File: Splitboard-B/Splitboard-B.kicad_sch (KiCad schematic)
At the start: 83 parts

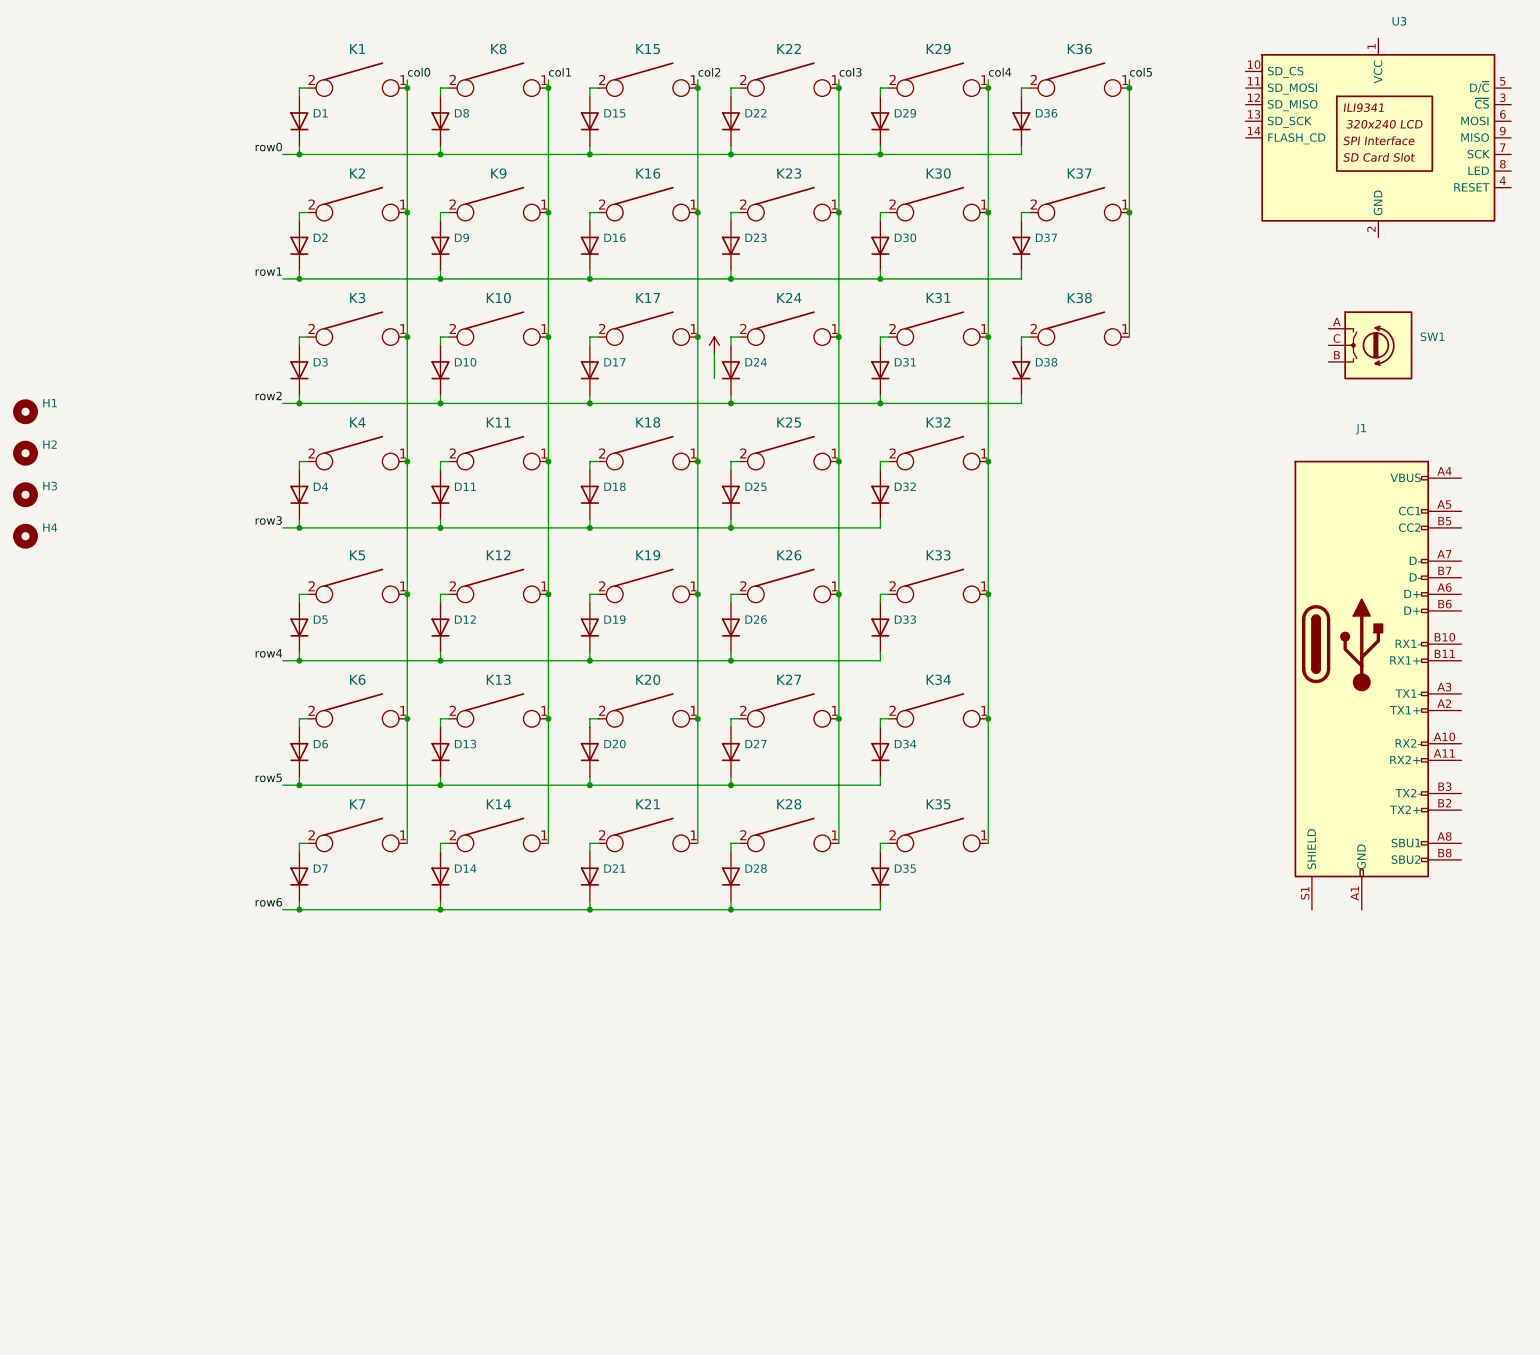
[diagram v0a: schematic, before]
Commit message: Keyboard changes (added split to other half, component footprints)
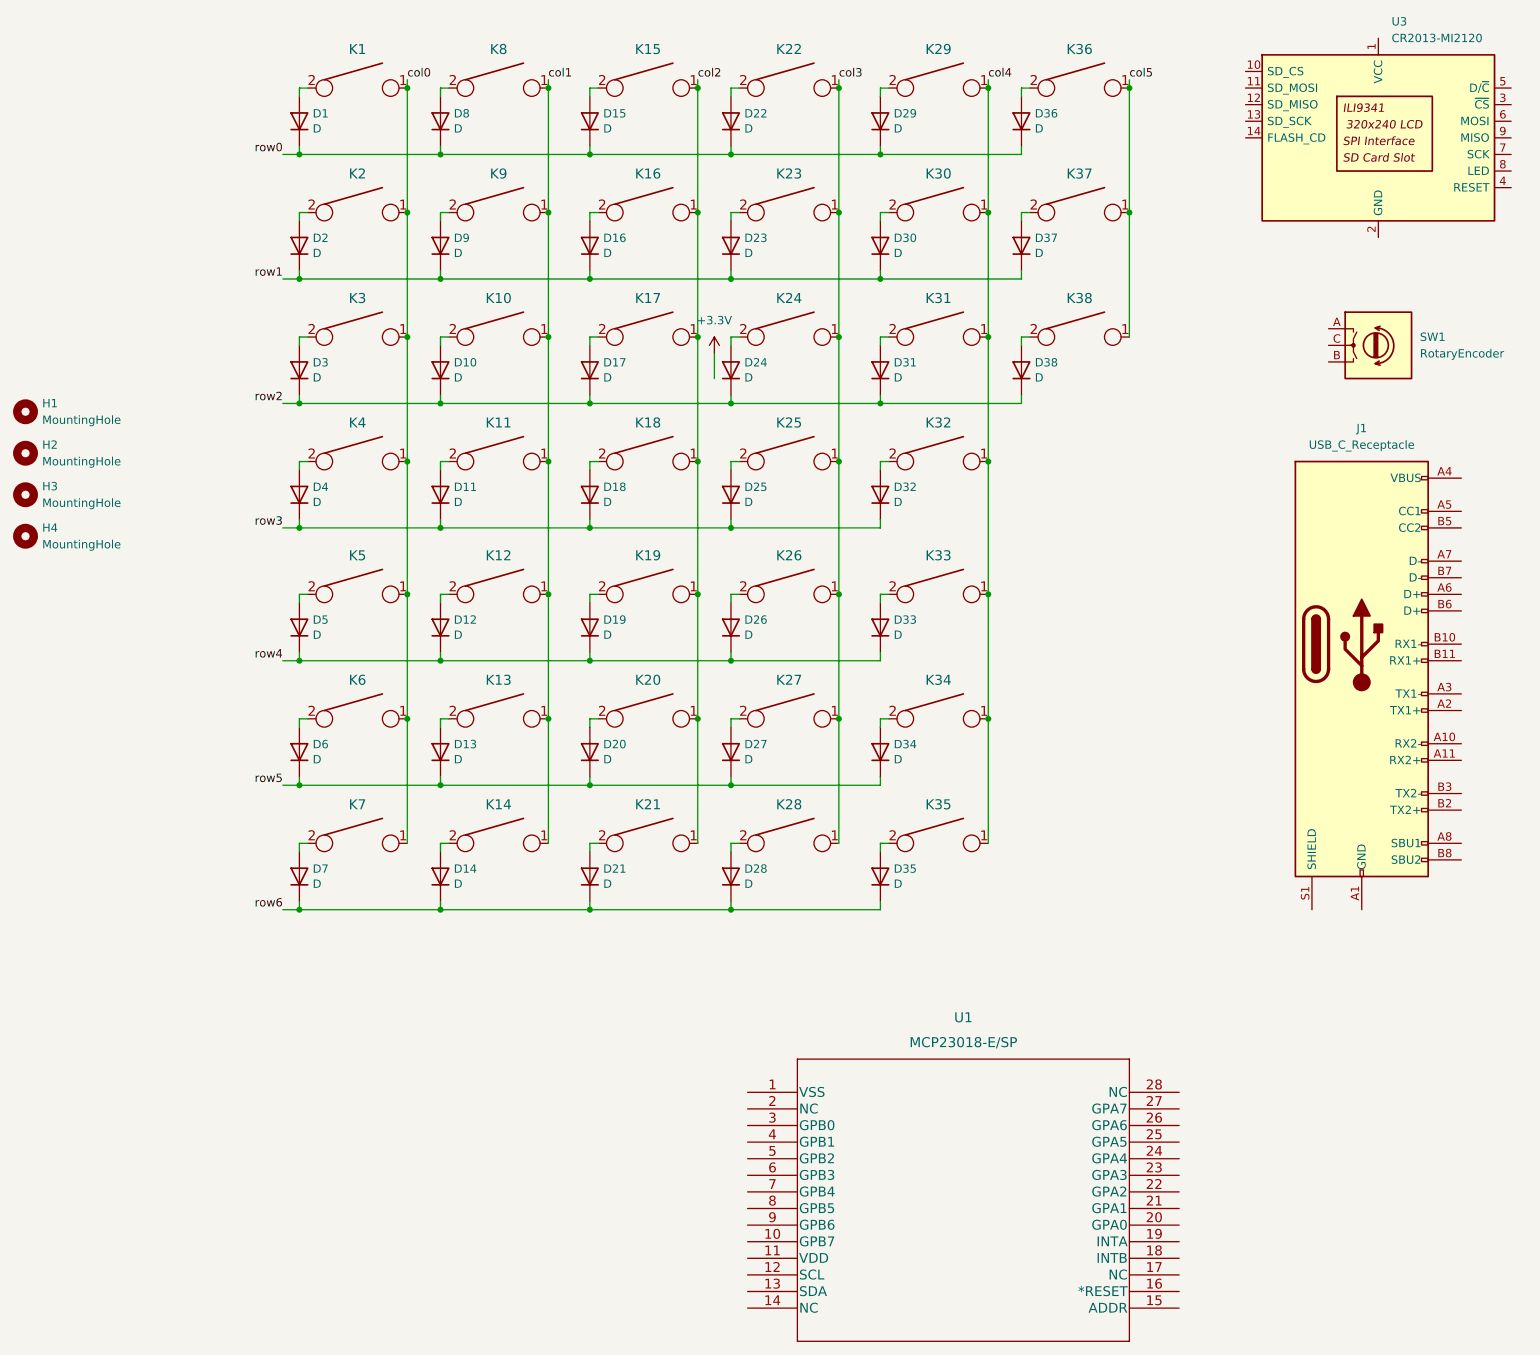
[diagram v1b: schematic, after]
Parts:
- added U1: MCP23018-E/SP, 6:MCP23018-E&slash_SP, symbol Interface_Expansion:MCP23018-E{brace}slash}SP
- D1, D10, D11, D12, D13, D14, D15, D16, D17, D18, D19, D2, D20, D21, D22, D23, D24, D25, D26, D27, D28, D29, D3, D30, D31, D32, D33, D34, D35, D36, D37, D38, D4, D5, D6, D7, D8, D9: value (none) -> D; footprint (none) -> Diode_SMD:D_SOD-123
- H1, H2, H3, H4: value (none) -> MountingHole; footprint (none) -> MountingHole:MountingHole_2.7mm
- J1: value (none) -> USB_C_Receptacle; footprint (none) -> USB_C_Receptacle_GCT_USB4085
- K1, K10, K11, K12, K13, K14, K15, K16, K17, K18, K19, K2, K20, K21, K22, K23, K24, K25, K26, K27, K28, K29, K3, K30, K31, K32, K33, K34, K35, K36, K37, K38, K4, K5, K6, K7, K8, K9: value (none) -> KEYSW; footprint (none) -> 6:SW_Hotswap_Kailh_MX_plated
- SW1: value (none) -> RotaryEncoder; footprint (none) -> Rotary_Encoder:RotaryEncoder_Alps_EC12E_Vertical_H20mm
- U3: value (none) -> CR2013-MI2120; footprint (none) -> Display:CR2013-MI2120

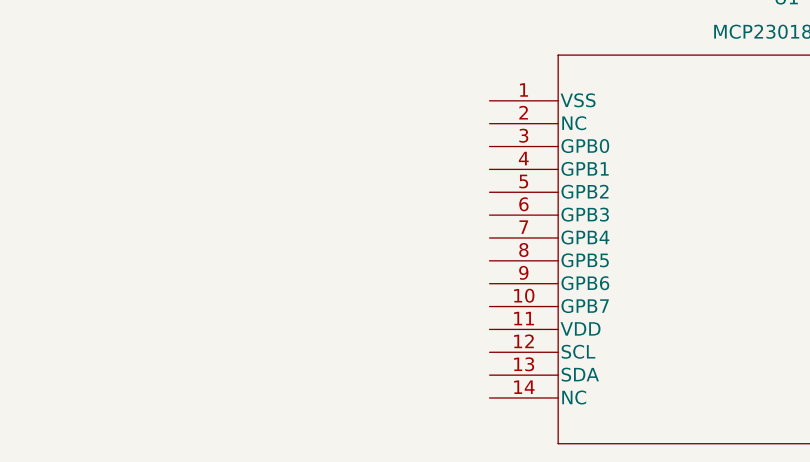
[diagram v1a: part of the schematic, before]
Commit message: added pullup resisitors
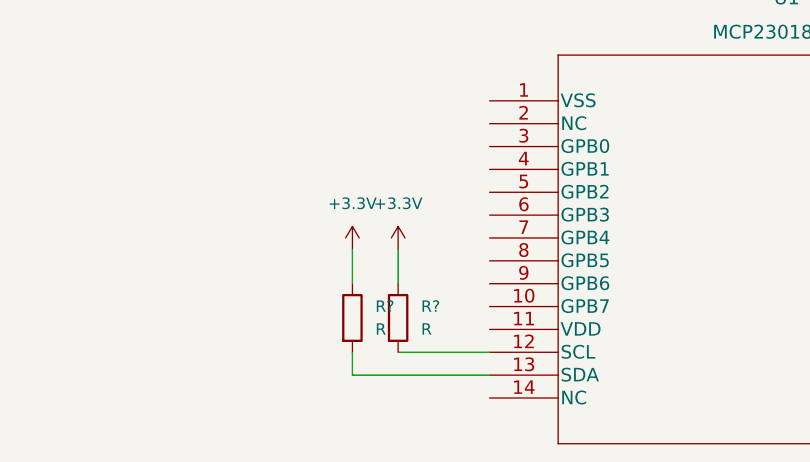
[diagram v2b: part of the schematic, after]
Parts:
- added R? (x2): R, symbol Device:R
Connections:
- net +3.3V: now also R?.1, R?.1
- net at U1.12 (SCL): now also R?.2
- net at U1.13 (SDA): now also R?.2
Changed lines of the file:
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@@
+    (stroke (width 0) (type default) (color 0 0 0 0))
+  )
+  (wire (pts (xy 133.35 218.44) (xy 118.11 218.44))
     (stroke (width 0) (type default) (color 0 0 0 0))
   )
@@
     (stroke (width 0) (type default) (color 0 0 0 0))
   )
+  (wire (pts (xy 123.19 204.47) (xy 123.19 208.28))
+    (stroke (width 0) (type default) (color 0 0 0 0))
+  )
   (wire (pts (xy 87.63 91.44) (xy 86.36 91.44))
     (stroke (width 0) (type default) (color 0 0 0 0))
@@
     (stroke (width 0) (type default) (color 0 0 0 0))
   )
+  (wire (pts (xy 118.11 215.9) (xy 118.11 218.44))
+    (stroke (width 0) (type default) (color 0 0 0 0))
+  )
   (wire (pts (xy 109.22 63.5) (xy 130.81 63.5))
     (stroke (width 0) (type default) (color 0 0 0 0))
@@
     (stroke (width 0) (type default) (color 0 0 0 0))
   )
+  (wire (pts (xy 123.19 215.9) (xy 133.35 215.9))
+    (stroke (width 0) (type default) (color 0 0 0 0))
+  )
   (wire (pts (xy 109.22 120.65) (xy 109.22 121.92))
     (stroke (width 0) (type default) (color 0 0 0 0))
@@
   )
   (wire (pts (xy 130.81 149.86) (xy 130.81 151.13))
+    (stroke (width 0) (type default) (color 0 0 0 0))
+  )
+  (wire (pts (xy 118.11 204.47) (xy 118.11 208.28))
     (stroke (width 0) (type default) (color 0 0 0 0))
   )
@@
     (pin "1")
     (pin "2")
+  )
+  (symbol (lib_id "power:+3.3V") (at 118.11 204.47 0) (unit 1)
+    (in_bom yes) (on_board yes) (fields_autoplaced)
+    (property "Reference" "#PWR?" (id 0) (at 118.11 208.28 0)
+      (effects (font (size 1.27 1.27)) hide)
+    )
+    (property "Value" "+3.3V" (id 1) (at 118.11 199.39 0))
+    (property "Footprint" "" (id 2) (at 118.11 204.47 0)
+      (effects (font (size 1.27 1.27)) hide)
+    )
+    (property "Datasheet" "" (id 3) (at 118.11 204.47 0)
+      (effects (font (size 1.27 1.27)) hide)
+    )
+    (pin "1")
   )
   (symbol (lib_id "KBT1-rescue:D-Device") (at 64.77 135.89 90) (unit 1)
@@
     (pin "2")
   )
+  (symbol (lib_id "power:+3.3V") (at 123.19 204.47 0) (unit 1)
+    (in_bom yes) (on_board yes) (fields_autoplaced)
+    (property "Reference" "#PWR?" (id 0) (at 123.19 208.28 0)
+      (effects (font (size 1.27 1.27)) hide)
+    )
+    (property "Value" "+3.3V" (id 1) (at 123.19 199.39 0))
+    (property "Footprint" "" (id 2) (at 123.19 204.47 0)
+      (effects (font (size 1.27 1.27)) hide)
+    )
+    (property "Datasheet" "" (id 3) (at 123.19 204.47 0)
+      (effects (font (size 1.27 1.27)) hide)
+    )
+    (pin "1")
+  )
   (symbol (lib_id "Mechanical:MountingHole") (at 22.86 96.52 0) (unit 1)
     (in_bom yes) (on_board yes) (fields_autoplaced)
@@
       (effects (font (size 1.27 1.27)) hide)
     )
+  )
+  (symbol (lib_id "Device:R") (at 118.11 212.09 0) (unit 1)
+    (in_bom yes) (on_board yes) (fields_autoplaced)
+    (property "Reference" "R?" (id 0) (at 120.65 210.8199 0)
+      (effects (font (size 1.27 1.27)) (justify left))
+    )
+    (property "Value" "R" (id 1) (at 120.65 213.3599 0)
+      (effects (font (size 1.27 1.27)) (justify left))
+    )
+    (property "Footprint" "" (id 2) (at 116.332 212.09 90)
+      (effects (font (size 1.27 1.27)) hide)
+    )
+    (property "Datasheet" "~" (id 3) (at 118.11 212.09 0)
+      (effects (font (size 1.27 1.27)) hide)
+    )
+    (pin "1")
+    (pin "2")
   )
   (symbol (lib_id "Mechanical:MountingHole") (at 22.86 102.87 0) (unit 1)
@@
     (property "Datasheet" "" (id 3) (at 162.56 53.34 0)
       (effects (font (size 1.524 1.524)))
+    )
+    (pin "1")
+    (pin "2")
+  )
+  (symbol (lib_id "Device:R") (at 123.19 212.09 0) (unit 1)
+    (in_bom yes) (on_board yes) (fields_autoplaced)
+    (property "Reference" "R?" (id 0) (at 125.73 210.8199 0)
+      (effects (font (size 1.27 1.27)) (justify left))
+    )
+    (property "Value" "R" (id 1) (at 125.73 213.3599 0)
+      (effects (font (size 1.27 1.27)) (justify left))
+    )
+    (property "Footprint" "" (id 2) (at 121.412 212.09 90)
+      (effects (font (size 1.27 1.27)) hide)
+    )
+    (property "Datasheet" "~" (id 3) (at 123.19 212.09 0)
+      (effects (font (size 1.27 1.27)) hide)
     )
     (pin "1")
@@
       (reference "#PWR0103") (unit 1) (value "+3.3V") (footprint "")
     )
+    (path "/31e77a53-3db0-43d9-8c57-a14833466fba"
+      (reference "#PWR?") (unit 1) (value "+3.3V") (footprint "")
+    )
+    (path "/5900d3e4-ddc5-4aff-8a88-379afa05c05c"
+      (reference "#PWR?") (unit 1) (value "+3.3V") (footprint "")
+    )
     (path "/00000000-0000-0000-0000-000060519a9d"
       (reference "D1") (unit 1) (value "D") (footprint "Diode_SMD:D_SOD-123")
@@
       (reference "K38") (unit 1) (value "KEYSW") (footprint "6:SW_Hotswap_Kailh_MX_plated")
     )
+    (path "/8e1772c9-43da-4b5a-bbb9-6939c65948ad"
+      (reference "R?") (unit 1) (value "R") (footprint "")
+    )
+    (path "/b4ddfeae-cfac-436b-bc28-3fcc02603ab9"
+      (reference "R?") (unit 1) (value "R") (footprint "")
+    )
     (path "/41c52e1b-e58e-4880-8477-e089c784c00c"
